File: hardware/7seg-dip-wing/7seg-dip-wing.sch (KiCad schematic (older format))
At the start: 8 parts, among them J1 Feather, SW1 SW_DIP_x08, U1 LTD-5623Ax, U2 74LVC2G17

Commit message: changes to make everything work with new library setup
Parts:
- added SW2: SW_SPDT, josh-buttons-switches:SW_SPDT_PCM12, symbol Switch:SW_SPDT
- J1: footprint josh-footprints:PCB_FeatherWing -> josh-connectors:featherwing; symbol josh-symbols:Feather -> 7seg-dip-wing-rescue:Feather-josh-symbols-7seg-dip-wing-rescue
- RN3, RN4: symbol josh-symbols:RN -> 7seg-dip-wing-rescue:RN-josh-symbols-7seg-dip-wing-rescue
- U1: symbol josh-symbols:LTD-5623Ax -> 7seg-dip-wing-rescue:LTD-5623Ax-josh-symbols-7seg-dip-wing-rescue
- U2: symbol josh-symbols:74LVC2G17 -> 7seg-dip-wing-rescue:74LVC2G17-josh-symbols-7seg-dip-wing-rescue
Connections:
- net +3V3: now also SW2.1 (A)
- net DIP_2: no longer J1.19 (IO13), J1.20 (IO14), RN2.5 (R4.2), RN2.6 (R3.2), SW1.3, SW1.4
- net GND: now also SW2.3 (C)
- net SWITCH: now reaches J1.25 (IO19)
- net SWITCH: now also SW2.2 (B)
- new net DIP_3: J1.19 (IO13), RN2.6 (R3.2), SW1.3
- new net DIP_4: J1.20 (IO14), RN2.5 (R4.2), SW1.4
- no-connect marks 7 -> 6
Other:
- moved on the sheet: RN1, RN2, RN3A, RN3B, RN3C, RN3D, RN4A, RN4B, RN4C, RN4D, SW1, U1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

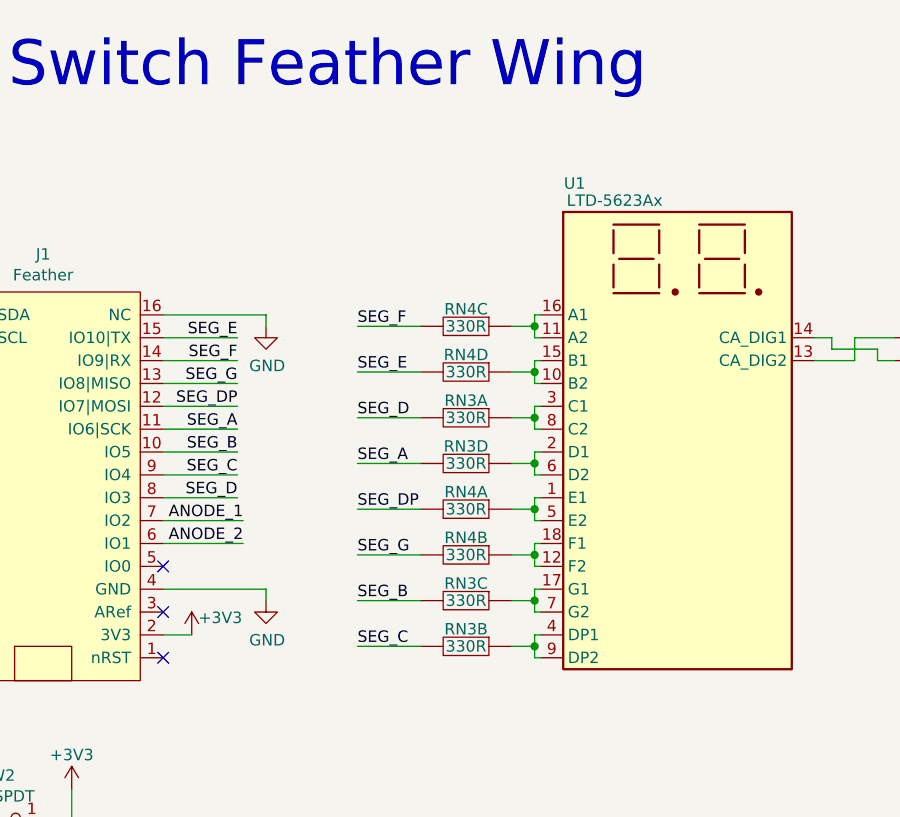
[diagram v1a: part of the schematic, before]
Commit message: fixing things which broke resulting from library change
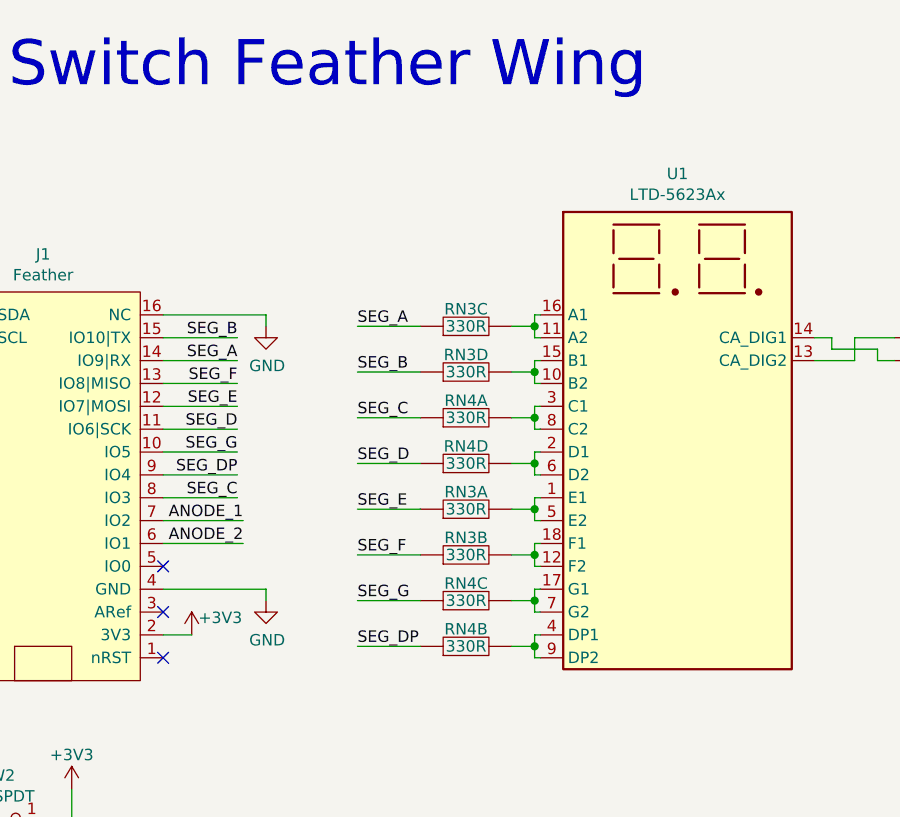
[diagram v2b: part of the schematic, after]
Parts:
- removed J1: Feather, josh-connectors:featherwing, symbol 7seg-dip-wing-rescue:Feather-josh-symbols-7seg-dip-wing-rescue
- removed RN3, RN4: 330R, Resistor_SMD:R_Array_Convex_4x0402, symbol 7seg-dip-wing-rescue:RN-josh-symbols-7seg-dip-wing-rescue
- removed U1: LTD-5623Ax, Display_7Segment:DA56-11SURKWA, symbol 7seg-dip-wing-rescue:LTD-5623Ax-josh-symbols-7seg-dip-wing-rescue
- removed U2: 74LVC2G17, Package_TO_SOT_SMD:SOT-363_SC-70-6, symbol 7seg-dip-wing-rescue:74LVC2G17-josh-symbols-7seg-dip-wing-rescue
- added J1: Feather, josh-connectors:featherwing, symbol josh-connector:Feather
- added RN3, RN4: 330R, Resistor_SMD:R_Array_Convex_4x0402, symbol josh-passive:RN
- added U1: LTD-5623Ax, Display_7Segment:DA56-11SEKWA, symbol josh-led:LTD-5623Ax
- added U2: 74LVC2G17, Package_TO_SOT_SMD:SOT-363_SC-70-6, symbol josh-logic:74LVC2G17
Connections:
- net +3V3: now also J1.2 (3V3), U2.5 (VCC)
- net ANODE_1: now also J1.7 (IO2), U2.1 (1A)
- net ANODE_2: now also J1.6 (IO1), U2.3 (2A)
- net DIP_1: now also J1.17 (IO11|SDA)
- net DIP_2: now also J1.18 (IO12|SCL)
- net DIP_3: now also J1.19 (IO13)
- net DIP_4: now also J1.20 (IO14)
- net DIP_5: now also J1.21 (IO15)
- net DIP_6: now also J1.22 (IO16)
- net DIP_7: now also J1.23 (IO17)
- net DIP_8: now also J1.24 (IO18)
- net GND: now also J1.16 (NC), J1.4 (GND), U2.2 (GND)
- net SEG_A: now also J1.14 (IO9|RX), RN3.2
- net SEG_B: now also J1.15 (IO10|TX), RN3.1
- net SEG_C: now also J1.8 (IO3), RN4.4
- net SEG_D: now also J1.11 (IO6|SCK), RN4.1
- net SEG_DP: now also J1.9 (IO4), RN4.3
- net SEG_E: now also J1.12 (IO7|MOSI), RN3.4
- net SEG_F: now also J1.13 (IO8|MISO), RN3.3
- net SEG_G: now also J1.10 (IO5), RN4.2
- net SWITCH: now also J1.25 (IO19)
- new net: RN3.5, U1.1 (E1), U1.5 (E2)
- new net: RN3.8, U1.10 (B2), U1.15 (B1)
- new net: RN3.7, U1.11 (A2), U1.16 (A1)
- new net: RN3.6, U1.12 (F2), U1.18 (F1)
- new net: U1.13 (CA_DIG2), U2.6 (1Y)
- new net: U1.14 (CA_DIG1), U2.4 (2Y)
- new net: RN4.7, U1.17 (G1), U1.7 (G2)
- new net: RN4.8, U1.2 (D1), U1.6 (D2)
- new net: RN4.5, U1.3 (C1), U1.8 (C2)
- new net: RN4.6, U1.4 (DP1), U1.9 (DP2)
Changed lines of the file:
@@
 	-1   0    0    -1
-$EndComp
-$Comp
-L 7seg-dip-wing-rescue:LTD-5623Ax-josh-symbols-7seg-dip-wing-rescue U1
-U 1 1 5D14A9DA
-P 8175 2175
-F 0 "U1" H 7725 2800 50  0000 C CNN
-F 1 "LTD-5623Ax" H 7900 2725 50  0000 C CNN
-F 2 "Display_7Segment:DA56-11SURKWA" H 8175 1575 50  0001 C CNN
-F 3 "https://docs.broadcom.com/docs/AV02-1589EN" H 7955 2275 50  0001 C CNN
-	1    8175 2175
-	1    0    0    -1
 $EndComp
 Wire Wire Line
@@
 Wire Wire Line
 	7550 2625 7575 2625
-Text Label 6775 3575 0    50   ~ 0
+Text Label 6775 2575 0    50   ~ 0
 SEG_C
 Wire Wire Line
@@
 Wire Wire Line
 	7550 2825 7575 2825
-Text Label 6775 2575 0    50   ~ 0
+Text Label 6775 2775 0    50   ~ 0
 SEG_D
 Wire Wire Line
@@
 Wire Wire Line
 	7550 3425 7575 3425
-Text Label 6775 3175 0    50   ~ 0
+Text Label 6775 3375 0    50   ~ 0
 SEG_G
 Wire Wire Line
@@
 Wire Wire Line
 	7550 3625 7575 3625
-$Comp
-L 7seg-dip-wing-rescue:Feather-josh-symbols-7seg-dip-wing-rescue J1
-U 1 1 5D163790
-P 5375 2825
-F 0 "J1" H 5400 3790 50  0000 C CNN
-F 1 "Feather" H 5400 3699 50  0000 C CNN
-F 2 "josh-connectors:featherwing" H 5575 1875 50  0001 C CNN
-F 3 "" H 5575 1875 50  0001 C CNN
-	1    5375 2825
-	1    0    0    -1
-$EndComp
 Text Notes 2975 1150 0    197  ~ 0
 7 Segment / DIP Switch Feather Wing
@@
 Text Label 10100 2325 2    50   ~ 0
 ANODE_2
+Text Label 6250 2325 2    50   ~ 0
+SEG_A
+Text Label 6250 2225 2    50   ~ 0
+SEG_B
+Text Label 6250 2925 2    50   ~ 0
+SEG_C
 Text Label 6250 2625 2    50   ~ 0
-SEG_A
+SEG_D
+Text Label 6250 2525 2    50   ~ 0
+SEG_E
+Text Label 6250 2425 2    50   ~ 0
+SEG_F
 Text Label 6250 2725 2    50   ~ 0
-SEG_B
+SEG_G
 Text Label 6250 2825 2    50   ~ 0
-SEG_C
-Text Label 6250 2925 2    50   ~ 0
-SEG_D
-Text Label 6250 2225 2    50   ~ 0
-SEG_E
-Text Label 6250 2325 2    50   ~ 0
-SEG_F
-Text Label 6250 2425 2    50   ~ 0
-SEG_G
-Text Label 6250 2525 2    50   ~ 0
 SEG_DP
 Wire Wire Line
@@
 Text Label 6275 3125 2    50   ~ 0
 ANODE_2
-$Comp
-L 7seg-dip-wing-rescue:74LVC2G17-josh-symbols-7seg-dip-wing-rescue U2
-U 1 1 5D1F9FB5
-P 9425 2275
-F 0 "U2" H 9450 2650 50  0000 C CNN
-F 1 "74LVC2G17" H 9450 2559 50  0000 C CNN
-F 2 "Package_TO_SOT_SMD:SOT-363_SC-70-6" H 9375 2525 197 0001 C CNN
-F 3 "" H 9375 2525 197 0001 C CNN
-	1    9425 2275
-	-1   0    0    -1
-$EndComp
 Wire Wire Line
 	9125 2225 8950 2225
@@
 Wire Wire Line
 	7550 3375 7550 3425
-$Comp
-L 7seg-dip-wing-rescue:RN-josh-symbols-7seg-dip-wing-rescue RN4
-U 2 1 5D3F3214
-P 7250 3175
-F 0 "RN4" V 7175 3175 50  0000 C CNN
-F 1 "330R" V 7250 3175 50  0000 C CNN
-F 2 "Resistor_SMD:R_Array_Convex_4x0402" H 7250 3175 50  0001 C CNN
-F 3 "~" H 7250 3175 50  0001 C CNN
-	2    7250 3175
-	0    1    1    0
-$EndComp
-$Comp
-L 7seg-dip-wing-rescue:RN-josh-symbols-7seg-dip-wing-rescue RN3
-U 2 1 5D3A93B0
-P 7250 3575
-F 0 "RN3" V 7175 3575 50  0000 C CNN
-F 1 "330R" V 7250 3575 50  0000 C CNN
-F 2 "Resistor_SMD:R_Array_Convex_4x0402" H 7250 3575 50  0001 C CNN
-F 3 "~" H 7250 3575 50  0001 C CNN
-	2    7250 3575
-	0    1    1    0
-$EndComp
-$Comp
-L 7seg-dip-wing-rescue:RN-josh-symbols-7seg-dip-wing-rescue RN3
-U 1 1 5D39AACC
-P 7250 2575
-F 0 "RN3" V 7175 2575 50  0000 C CNN
-F 1 "330R" V 7250 2575 50  0000 C CNN
-F 2 "Resistor_SMD:R_Array_Convex_4x0402" H 7250 2575 50  0001 C CNN
-F 3 "~" H 7250 2575 50  0001 C CNN
-	1    7250 2575
-	0    1    1    0
-$EndComp
-Text Label 6775 3375 0    50   ~ 0
+Text Label 6775 2375 0    50   ~ 0
 SEG_B
 Wire Wire Line
 	7050 3375 6775 3375
-$Comp
-L 7seg-dip-wing-rescue:RN-josh-symbols-7seg-dip-wing-rescue RN3
-U 3 1 5D3AA440
-P 7250 3375
-F 0 "RN3" V 7175 3375 50  0000 C CNN
-F 1 "330R" V 7250 3375 50  0000 C CNN
-F 2 "Resistor_SMD:R_Array_Convex_4x0402" H 7250 3375 50  0001 C CNN
-F 3 "~" H 7250 3375 50  0001 C CNN
-	3    7250 3375
-	0    1    1    0
-$EndComp
-Text Label 6775 2775 0    50   ~ 0
+Text Label 6775 2175 0    50   ~ 0
 SEG_A
 Wire Wire Line
 	6775 2775 7050 2775
-$Comp
-L 7seg-dip-wing-rescue:RN-josh-symbols-7seg-dip-wing-rescue RN3
-U 4 1 5D3AAE3C
-P 7250 2775
-F 0 "RN3" V 7175 2775 50  0000 C CNN
-F 1 "330R" V 7250 2775 50  0000 C CNN
-F 2 "Resistor_SMD:R_Array_Convex_4x0402" H 7250 2775 50  0001 C CNN
-F 3 "~" H 7250 2775 50  0001 C CNN
-	4    7250 2775
-	0    1    1    0
-$EndComp
-Text Label 6775 2175 0    50   ~ 0
+Text Label 6775 3175 0    50   ~ 0
 SEG_F
 Wire Wire Line
-	7050 2175 6775 2175
-$Comp
-L 7seg-dip-wing-rescue:RN-josh-symbols-7seg-dip-wing-rescue RN4
-U 3 1 5D3F321A
-P 7250 2175
-F 0 "RN4" V 7175 2175 50  0000 C CNN
-F 1 "330R" V 7250 2175 50  0000 C CNN
-F 2 "Resistor_SMD:R_Array_Convex_4x0402" H 7250 2175 50  0001 C CNN
-F 3 "~" H 7250 2175 50  0001 C CNN
-	3    7250 2175
-	0    1    1    0
-$EndComp
-$Comp
-L 7seg-dip-wing-rescue:RN-josh-symbols-7seg-dip-wing-rescue RN4
-U 1 1 5D3F320E
-P 7250 2975
-F 0 "RN4" V 7175 2975 50  0000 C CNN
-F 1 "330R" V 7250 2975 50  0000 C CNN
-F 2 "Resistor_SMD:R_Array_Convex_4x0402" H 7250 2975 50  0001 C CNN
-F 3 "~" H 7250 2975 50  0001 C CNN
-	1    7250 2975
-	0    1    1    0
-$EndComp
-Wire Wire Line
 	7050 2975 6775 2975
-Text Label 6775 2975 0    50   ~ 0
+Text Label 6775 3575 0    50   ~ 0
 SEG_DP
 Connection ~ 7550 2375
@@
 Wire Wire Line
 	6775 2375 7050 2375
-$Comp
-L 7seg-dip-wing-rescue:RN-josh-symbols-7seg-dip-wing-rescue RN4
-U 4 1 5D3F3220
-P 7250 2375
-F 0 "RN4" V 7175 2375 50  0000 C CNN
-F 1 "330R" V 7250 2375 50  0000 C CNN
-F 2 "Resistor_SMD:R_Array_Convex_4x0402" H 7250 2375 50  0001 C CNN
-F 3 "~" H 7250 2375 50  0001 C CNN
-	4    7250 2375
-	0    1    1    0
-$EndComp
-Text Label 6775 2375 0    50   ~ 0
+Text Label 6775 2975 0    50   ~ 0
 SEG_E
 Wire Wire Line
@@
 Wire Wire Line
 	4050 2225 4050 2950
+$Comp
+L josh-connector:Feather J1
+U 1 1 5D175B15
+P 5375 2825
+F 0 "J1" H 5400 3790 50  0000 C CNN
+F 1 "Feather" H 5400 3699 50  0000 C CNN
+F 2 "josh-connectors:featherwing" H 5575 1875 50  0001 C CNN
+F 3 "" H 5575 1875 50  0001 C CNN
+	1    5375 2825
+	1    0    0    -1
+$EndComp
+$Comp
+L josh-led:LTD-5623Ax U1
+U 1 1 5D176950
+P 8175 2175
+F 0 "U1" H 8175 2842 50  0000 C CNN
+F 1 "LTD-5623Ax" H 8175 2751 50  0000 C CNN
+F 2 "Display_7Segment:DA56-11SEKWA" H 8175 1575 50  0001 C CNN
+F 3 "https://docs.broadcom.com/docs/AV02-1589EN" H 7955 2275 50  0001 C CNN
+	1    8175 2175
+	1    0    0    -1
+$EndComp
+$Comp
+L josh-logic:74LVC2G17 U2
+U 1 1 5D177631
+P 9425 2275
+F 0 "U2" H 9450 2650 50  0000 C CNN
+F 1 "74LVC2G17" H 9450 2559 50  0000 C CNN
+F 2 "Package_TO_SOT_SMD:SOT-363_SC-70-6" H 9375 2525 197 0001 C CNN
+F 3 "" H 9375 2525 197 0001 C CNN
+	1    9425 2275
+	-1   0    0    -1
+$EndComp
+Wire Wire Line
+	6775 2175 7050 2175
+$Comp
+L josh-passive:RN RN3
+U 1 1 5D230879
+P 7250 2975
+F 0 "RN3" H 7250 3050 50  0000 C CNN
+F 1 "330R" H 7250 2975 50  0000 C CNN
+F 2 "Resistor_SMD:R_Array_Convex_4x0402" V 7250 2975 50  0001 C CNN
+F 3 "~" V 7250 2975 50  0001 C CNN
+	1    7250 2975
+	1    0    0    -1
+$EndComp
+$Comp
+L josh-passive:RN RN3
+U 2 1 5D230E31
+P 7250 3175
+F 0 "RN3" H 7250 3250 50  0000 C CNN
+F 1 "330R" H 7250 3175 50  0000 C CNN
+F 2 "Resistor_SMD:R_Array_Convex_4x0402" V 7250 3175 50  0001 C CNN
+F 3 "~" V 7250 3175 50  0001 C CNN
+	2    7250 3175
+	1    0    0    -1
+$EndComp
+$Comp
+L josh-passive:RN RN3
+U 3 1 5D2314FF
+P 7250 2175
+F 0 "RN3" H 7250 2250 50  0000 C CNN
+F 1 "330R" H 7250 2175 50  0000 C CNN
+F 2 "Resistor_SMD:R_Array_Convex_4x0402" V 7250 2175 50  0001 C CNN
+F 3 "~" V 7250 2175 50  0001 C CNN
+	3    7250 2175
+	1    0    0    -1
+$EndComp
+$Comp
+L josh-passive:RN RN3
+U 4 1 5D231D9A
+P 7250 2375
+F 0 "RN3" H 7250 2450 50  0000 C CNN
+F 1 "330R" H 7250 2375 50  0000 C CNN
+F 2 "Resistor_SMD:R_Array_Convex_4x0402" V 7250 2375 50  0001 C CNN
+F 3 "~" V 7250 2375 50  0001 C CNN
+	4    7250 2375
+	1    0    0    -1
+$EndComp
+$Comp
+L josh-passive:RN RN4
+U 1 1 5D243933
+P 7250 2575
+F 0 "RN4" H 7250 2650 50  0000 C CNN
+F 1 "330R" H 7250 2575 50  0000 C CNN
+F 2 "Resistor_SMD:R_Array_Convex_4x0402" V 7250 2575 50  0001 C CNN
+F 3 "~" V 7250 2575 50  0001 C CNN
+	1    7250 2575
+	1    0    0    -1
+$EndComp
+$Comp
+L josh-passive:RN RN4
+U 2 1 5D243939
+P 7250 3575
+F 0 "RN4" H 7250 3650 50  0000 C CNN
+F 1 "330R" H 7250 3575 50  0000 C CNN
+F 2 "Resistor_SMD:R_Array_Convex_4x0402" V 7250 3575 50  0001 C CNN
+F 3 "~" V 7250 3575 50  0001 C CNN
+	2    7250 3575
+	1    0    0    -1
+$EndComp
+$Comp
+L josh-passive:RN RN4
+U 3 1 5D24393F
+P 7250 3375
+F 0 "RN4" H 7250 3450 50  0000 C CNN
+F 1 "330R" H 7250 3375 50  0000 C CNN
+F 2 "Resistor_SMD:R_Array_Convex_4x0402" V 7250 3375 50  0001 C CNN
+F 3 "~" V 7250 3375 50  0001 C CNN
+	3    7250 3375
+	1    0    0    -1
+$EndComp
+$Comp
+L josh-passive:RN RN4
+U 4 1 5D243945
+P 7250 2775
+F 0 "RN4" H 7250 2850 50  0000 C CNN
+F 1 "330R" H 7250 2775 50  0000 C CNN
+F 2 "Resistor_SMD:R_Array_Convex_4x0402" V 7250 2775 50  0001 C CNN
+F 3 "~" V 7250 2775 50  0001 C CNN
+	4    7250 2775
+	1    0    0    -1
+$EndComp
 $EndSCHEMATC

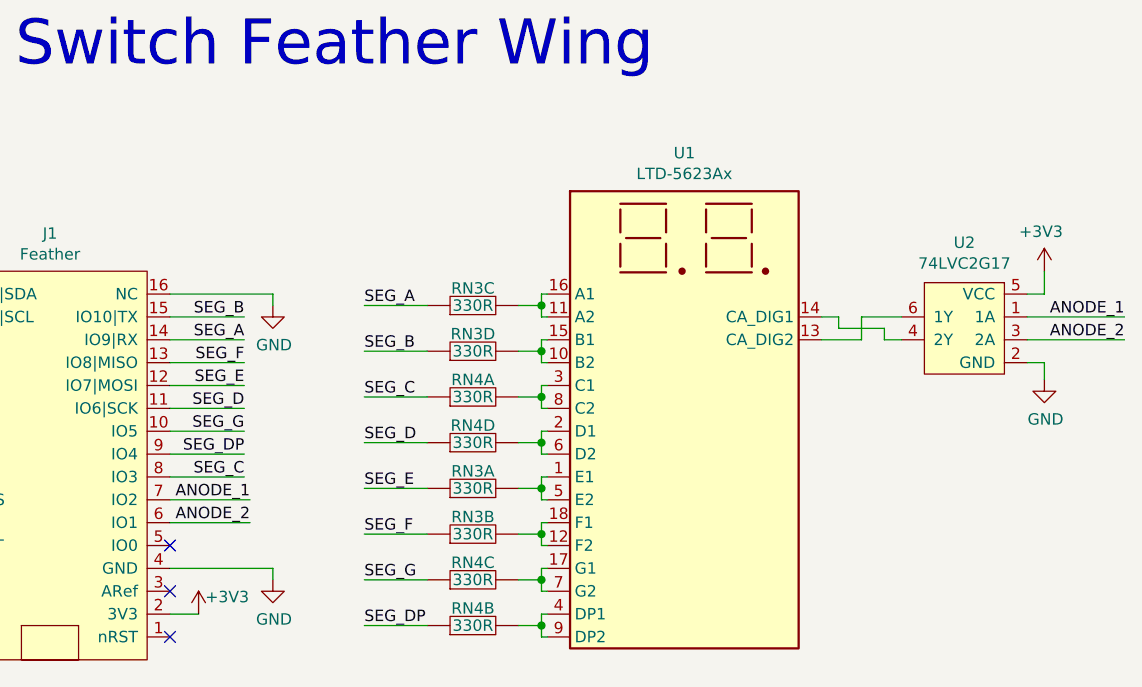
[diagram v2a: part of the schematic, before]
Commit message: updated seven seg schematic
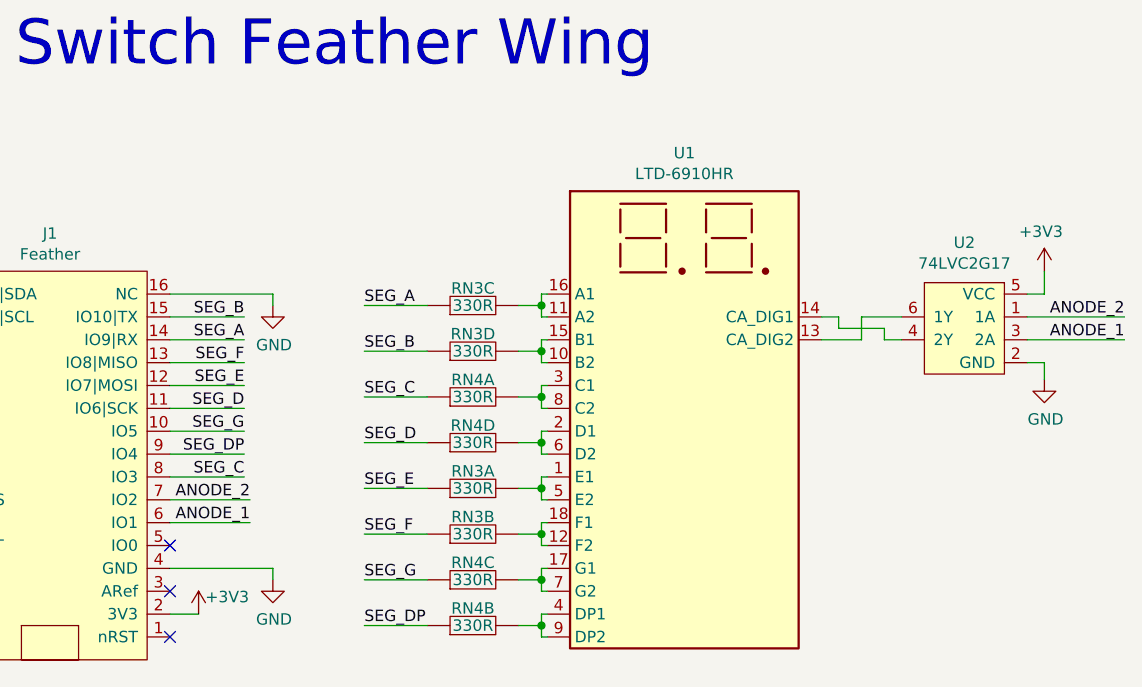
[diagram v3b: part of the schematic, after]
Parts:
- U1: value LTD-5623Ax -> LTD-6910HR
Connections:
- net ANODE_1: now also J1.6 (IO1), U2.3 (2A); no longer J1.7 (IO2), U2.1 (1A)
- net ANODE_2: now also J1.7 (IO2), U2.1 (1A); no longer J1.6 (IO1), U2.3 (2A)
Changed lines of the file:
@@
 Wire Wire Line
 	9675 2325 10100 2325
+Text Label 10100 2325 2    50   ~ 0
+ANODE_1
 Text Label 10100 2225 2    50   ~ 0
-ANODE_1
-Text Label 10100 2325 2    50   ~ 0
 ANODE_2
 Text Label 6250 2325 2    50   ~ 0
@@
 Wire Wire Line
 	5925 3125 6275 3125
+Text Label 6275 3125 2    50   ~ 0
+ANODE_1
 Text Label 6275 3025 2    50   ~ 0
-ANODE_1
-Text Label 6275 3125 2    50   ~ 0
 ANODE_2
 Wire Wire Line
@@
 P 8175 2175
 F 0 "U1" H 8175 2842 50  0000 C CNN
-F 1 "LTD-5623Ax" H 8175 2751 50  0000 C CNN
+F 1 "LTD-6910HR" H 8175 2751 50  0000 C CNN
 F 2 "Display_7Segment:DA56-11SEKWA" H 8175 1575 50  0001 C CNN
 F 3 "https://docs.broadcom.com/docs/AV02-1589EN" H 7955 2275 50  0001 C CNN
